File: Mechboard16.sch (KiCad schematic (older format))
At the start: 133 parts, among them CN1 CONN_C16, CN2 CONN_+4, SW0:0 KEY_DEL, SW0:1 KEY_RET, SW0:2 KEY_PND, SW0:3 KEY_HLP, SW0:4 KEY_F1, SW0:5 KEY_F2, SW0:6 KEY_F3, SW0:7 KEY_AT, SW1:0 KEY_3, SW1:1 KEY_W, SW1:2 KEY_A, SW1:3 KEY_4, SW1:4 KEY_Z, SW1:5 KEY_S, SW1:6 KEY_E, SW1:7 KEY_LSH, SW1B:7 KEY_RSH, SW1C:7 KEY_CLK, SW2:0 KEY_5, SW2:1 KEY_R, SW2:2 KEY_D, SW2:3 KEY_6, SW2:4 KEY_C, SW2:5 KEY_F, SW2:6 KEY_T, SW2:7 KEY_X, SW3:0 KEY_7, SW3:1 KEY_Y, SW3:2 KEY_G, SW3:3 KEY_8, SW3:4 KEY_B, SW3:5 KEY_H, SW3:6 KEY_U, SW3:7 KEY_V, SW4:0 KEY_9, SW4:1 KEY_I, SW4:2 KEY_J, SW4:3 KEY_0, SW4:4 KEY_M, SW4:5 KEY_K, SW4:6 KEY_O, SW4:7 KEY_N, SW5:0 KEY_DN, SW5:1 KEY_P, SW5:2 KEY_L, SW5:3 KEY_UP, SW5:4 KEY_DOT, SW5:5 KEY_COL, SW5:6 KEY_MIN, SW5:7 KEY_COM, SW6:0 KEY_LF, SW6:1 KEY_AST, SW6:2 KEY_SEM, SW6:3 KEY_RT, SW6:4 KEY_ESC, SW6:5 KEY_EQ, SW6:6 KEY_PLS, SW6:7 KEY_SLA, SW7:0 KEY_1, SW7:1 KEY_CLR, SW7:2 KEY_CTL, SW7:3 KEY_2, SW7:4 KEY_SPC, SW7:5 KEY_CMD, SW7:6 KEY_Q, SW7:7 KEY_RUN

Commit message: Schematics should be final
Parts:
- added C1, C2: 100n, Capacitor_SMD:C_0805_2012Metric_Pad1.18x1.45mm_HandSolder, symbol Device:C
- added C3: 10n, Capacitor_SMD:C_0805_2012Metric_Pad1.18x1.45mm_HandSolder, symbol Device:C
- added C4: 1u, Capacitor_THT:CP_Radial_D5.0mm_P2.00mm, symbol Device:CP1
- added JP2: JMP_SHIFTLOCK, Connector_PinHeader_2.54mm:PinHeader_2x03_P2.54mm_Vertical, symbol Connector_Generic:Conn_02x03_Odd_Even
- added LD1: LED, LED_THT:LED_D3.0mm, symbol Device:LED
- added R1, R4: 10k, Resistor_SMD:R_0805_2012Metric_Pad1.20x1.40mm_HandSolder, symbol Device:R
- added R2: 100k, Resistor_SMD:R_0805_2012Metric_Pad1.20x1.40mm_HandSolder, symbol Device:R
- added R3: 56, Resistor_SMD:R_0805_2012Metric_Pad1.20x1.40mm_HandSolder, symbol Device:R
- added U1: 4066, Package_SO:SOIC-14_3.9x8.7mm_P1.27mm, symbol 4xxx:4066
- added U2: NE555, Package_SO:SOIC-8_3.9x4.9mm_P1.27mm, symbol Timer:NE555D
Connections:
- net +5V: now also C1.1, C2.1, R1.2, U1.14 (VDD), U2.4 (R), U2.8 (VCC)
- net GND: now also C1.2, C2.2, C3.2, C4.2, LD1.1 (K), R4.1, U1.12, U1.5, U1.6, U1.7 (VSS), U2.1 (GND)
- net col7: now also JP2.4 (Pin_4)
- net row1: now also JP2.3 (Pin_3); no longer SW1C:7.1
- net at D1:7.2 (A), SW1:7.2, SW1B:7.2: no longer SW1C:7.2
- new net: C4.1, JP2.1 (Pin_1), R2.1, SW1C:7.1
- new net: JP2.2 (Pin_2), R1.1, R4.2, SW1C:7.2, U2.2 (TR), U2.6 (THR)
- new net: JP2.6 (Pin_6), U1.1
- new net: R2.2, R3.2, U1.13, U2.3 (Q)
- new net: JP2.5 (Pin_5), U1.2
- new net: LD1.2 (A), R3.1
- new net: C3.1, U2.5 (CV)
- no-connect marks 2 -> 9
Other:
- note added: ""MOMENTARY" TO "LATCHING" CIRCUIT\nFOR THE SHIFT LOCK KEY"
- note added: "Both Shift keys and\nCaps Lock are in parallel\n(But we handle the latter\nseparately so that we can\nuse a non-latching switch)"
- note added: "COMPUTER CONNECTORS"
- note added: "DECOUPLING"
- note added: "KEYBOARD MATRIX"
- note added: "Note that the C16 does not\nhave power on the keyboard\nconnector! A bodge wire mod\nwill be needed!\nFor LittleSixteen, we'll add a\njumper in the next release."
- note added: "SET JP2 ACCORDING TO TYPE\nOF SW1C:7:\n- LATCHING: 1-3 + 2-4\n- MOMENTARY: 3-5 + 4-6"
- note added: "SPARES"
- note added: "Yeah, having the +4 connector here doesn't make much\nsense, since the +4 keyboard uses a totally different form\nfactor, but we get it basically for free and it might still be\ngood for temporary use or whatever."
- moved on the sheet: CN1, CN2, D0:0, D0:1, D0:2, D0:3, D0:4, D0:5, D0:6, D0:7, D1:0, D1:1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

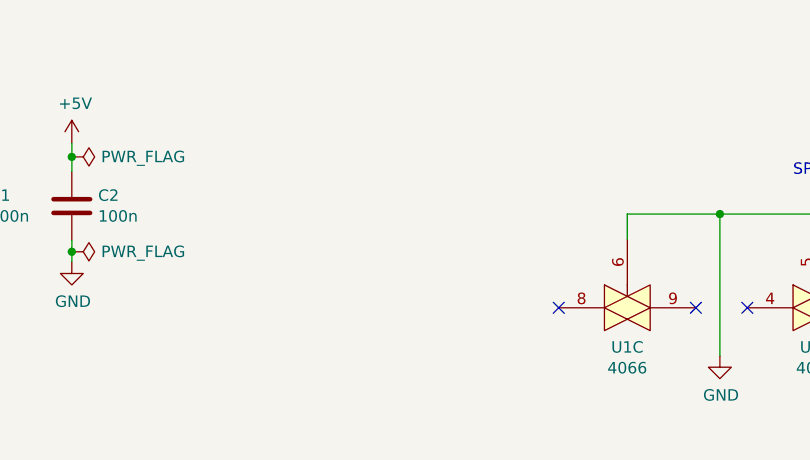
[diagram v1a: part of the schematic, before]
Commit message: Add screw holes
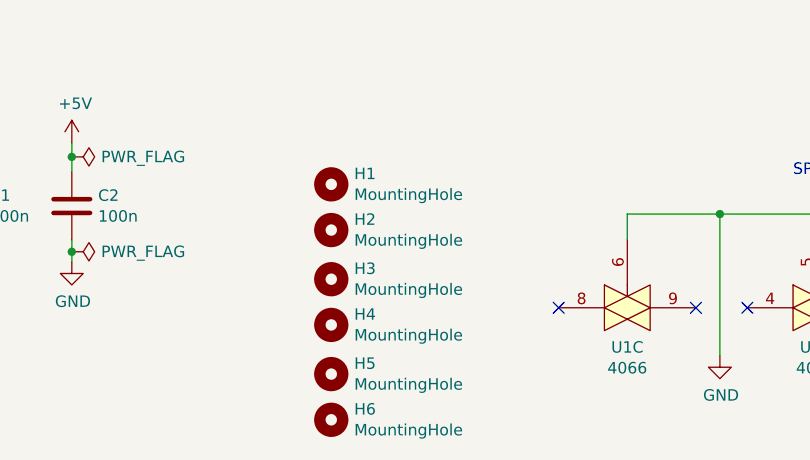
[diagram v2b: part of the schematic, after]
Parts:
- added H1, H2, H3, H4, H5, H6: MountingHole, MountingHole:MountingHole_3.5mm, symbol Mechanical:MountingHole
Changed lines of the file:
@@
 Text Notes 8205 1225 2    50   ~ 0
 Note that the C16 does not\nhave power on the keyboard\nconnector! A bodge wire mod\nwill be needed!\nFor LittleSixteen, we'll add a\njumper in the next release.
+$Comp
+L Mechanical:MountingHole H4
+U 1 1 68545552
+P 3385 7200
+F 0 "H4" H 3485 7246 50  0000 L CNN
+F 1 "MountingHole" H 3485 7155 50  0000 L CNN
+F 2 "MountingHole:MountingHole_3.5mm" H 3385 7200 50  0001 C CNN
+F 3 "~" H 3385 7200 50  0001 C CNN
+	1    3385 7200
+	1    0    0    -1
+$EndComp
+$Comp
+L Mechanical:MountingHole H3
+U 1 1 68546123
+P 3385 7000
+F 0 "H3" H 3485 7046 50  0000 L CNN
+F 1 "MountingHole" H 3485 6955 50  0000 L CNN
+F 2 "MountingHole:MountingHole_3.5mm" H 3385 7000 50  0001 C CNN
+F 3 "~" H 3385 7000 50  0001 C CNN
+	1    3385 7000
+	1    0    0    -1
+$EndComp
+$Comp
+L Mechanical:MountingHole H2
+U 1 1 685466B6
+P 3385 6785
+F 0 "H2" H 3485 6831 50  0000 L CNN
+F 1 "MountingHole" H 3485 6740 50  0000 L CNN
+F 2 "MountingHole:MountingHole_3.5mm" H 3385 6785 50  0001 C CNN
+F 3 "~" H 3385 6785 50  0001 C CNN
+	1    3385 6785
+	1    0    0    -1
+$EndComp
+$Comp
+L Mechanical:MountingHole H1
+U 1 1 68547692
+P 3385 6585
+F 0 "H1" H 3485 6631 50  0000 L CNN
+F 1 "MountingHole" H 3485 6540 50  0000 L CNN
+F 2 "MountingHole:MountingHole_3.5mm" H 3385 6585 50  0001 C CNN
+F 3 "~" H 3385 6585 50  0001 C CNN
+	1    3385 6585
+	1    0    0    -1
+$EndComp
+$Comp
+L Mechanical:MountingHole H6
+U 1 1 685F01A9
+P 3385 7615
+F 0 "H6" H 3485 7661 50  0000 L CNN
+F 1 "MountingHole" H 3485 7570 50  0000 L CNN
+F 2 "MountingHole:MountingHole_3.5mm" H 3385 7615 50  0001 C CNN
+F 3 "~" H 3385 7615 50  0001 C CNN
+	1    3385 7615
+	1    0    0    -1
+$EndComp
+$Comp
+L Mechanical:MountingHole H5
+U 1 1 685F119D
+P 3385 7415
+F 0 "H5" H 3485 7461 50  0000 L CNN
+F 1 "MountingHole" H 3485 7370 50  0000 L CNN
+F 2 "MountingHole:MountingHole_3.5mm" H 3385 7415 50  0001 C CNN
+F 3 "~" H 3385 7415 50  0001 C CNN
+	1    3385 7415
+	1    0    0    -1
+$EndComp
 $EndSCHEMATC

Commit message: Routing done
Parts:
- CN1: footprint Connector_PinHeader_2.54mm:PinHeader_1x20_P2.54mm_Horizontal -> Connector_PinHeader_2.54mm:PinHeader_1x20_P2.54mm_Vertical
- CN2: footprint Connector_PinHeader_2.54mm:PinHeader_1x18_P2.54mm_Horizontal -> Connector_PinHeader_2.54mm:PinHeader_1x18_P2.54mm_Vertical
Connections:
- net col7: no longer JP2.4 (Pin_4)
- net shift_b: now reaches D1:7.2 (A), SW1:7.2, SW1B:7.2
- net shift_b: now also JP2.4 (Pin_4)
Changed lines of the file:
@@
 Comp "SukkoPera"
 Comment1 "Mechanical replacement keyboard for the Commodore 16"
-Comment2 ""
+Comment2 "https://github.com/SukkoPera/MechBoard16"
 Comment3 "Heavily inspired by MechBoard64 by MtnBuffalo"
 Comment4 "https://www.breadbox64.com/blog/the-mechboard64/"
@@
 F 0 "CN2" H 10337 1954 50  0000 R CNN
 F 1 "CONN_+4" H 10337 1863 50  0000 R CNN
-F 2 "Connector_PinHeader_2.54mm:PinHeader_1x18_P2.54mm_Horizontal" H 10365 1980 50  0001 C CNN
+F 2 "Connector_PinHeader_2.54mm:PinHeader_1x18_P2.54mm_Vertical" H 10365 1980 50  0001 C CNN
 F 3 "~" H 10365 1980 50  0001 C CNN
 	1    10365 1980
@@
 F 0 "CN1" H 8977 2054 50  0000 R CNN
 F 1 "CONN_C16" H 8977 1963 50  0000 R CNN
-F 2 "Connector_PinHeader_2.54mm:PinHeader_1x20_P2.54mm_Horizontal" H 9005 2080 50  0001 C CNN
+F 2 "Connector_PinHeader_2.54mm:PinHeader_1x20_P2.54mm_Vertical" H 9005 2080 50  0001 C CNN
 F 3 "~" H 9005 2080 50  0001 C CNN
 	1    9005 2080
@@
 SPARES
 Text Label 10810 4615 2    50   ~ 0
-col7
+shift_b
 Text Label 9705 4615 0    50   ~ 0
-row1
+shift_a
 Wire Wire Line
 	10490 4515 10585 4515
@@
 	1    0    0    -1
 $EndComp
+Text Label 5675 1835 2    50   ~ 0
+shift_a
+Text Label 5875 2235 2    50   ~ 0
+shift_b
 $EndSCHEMATC

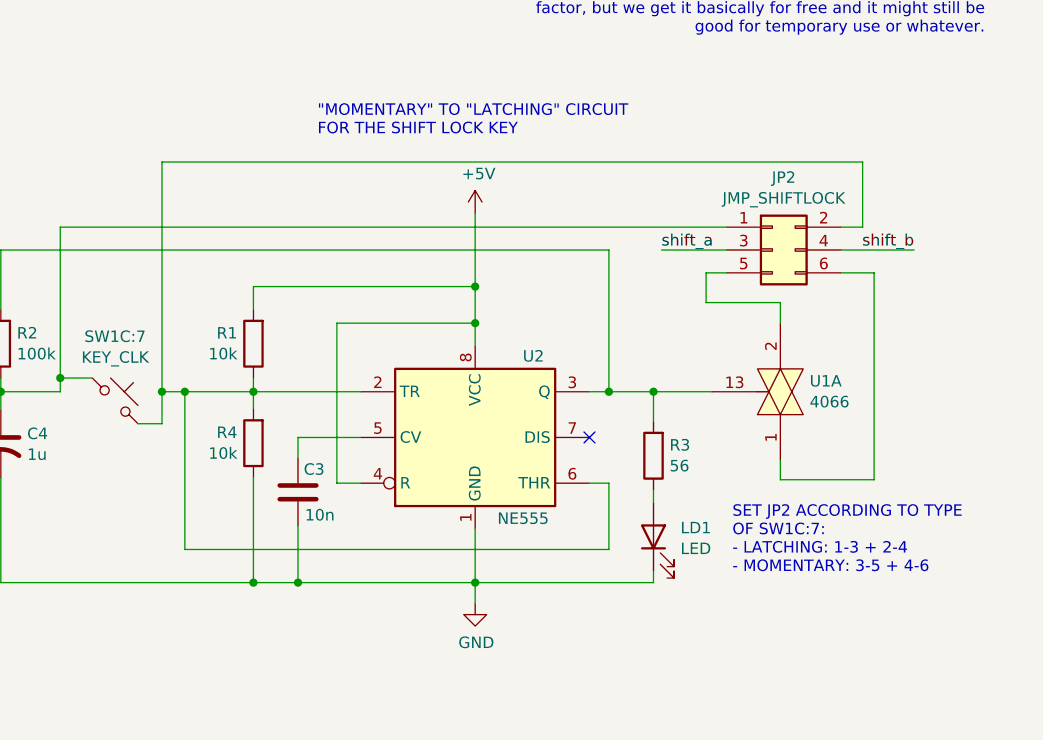
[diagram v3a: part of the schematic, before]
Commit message: Change JP2 to solder jumper(s)
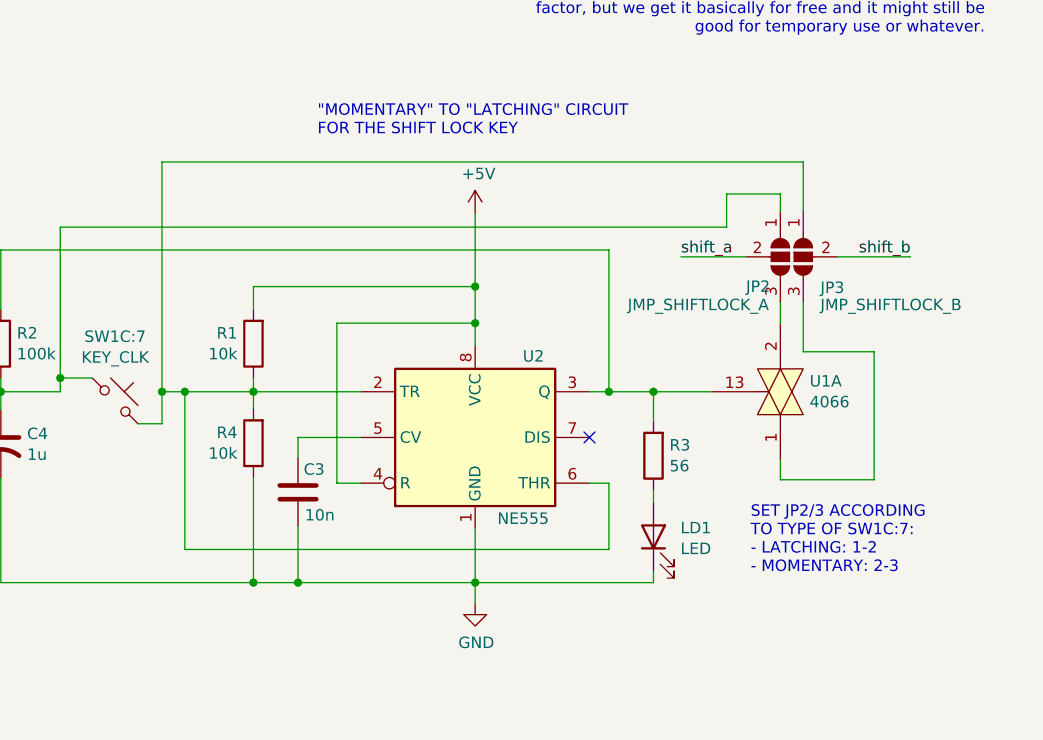
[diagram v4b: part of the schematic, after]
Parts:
- removed JP2: JMP_SHIFTLOCK, Connector_PinHeader_2.54mm:PinHeader_2x03_P2.54mm_Vertical, symbol Connector_Generic:Conn_02x03_Odd_Even
- added JP2: JMP_SHIFTLOCK_A, Jumper:SolderJumper-3_P1.3mm_Open_RoundedPad1.0x1.5mm, symbol Jumper:SolderJumper_3_Open
- added JP3: JMP_SHIFTLOCK_B, Jumper:SolderJumper-3_P1.3mm_Open_RoundedPad1.0x1.5mm, symbol Jumper:SolderJumper_3_Open
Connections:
- net row1: now also JP3.2 (C)
- net shift_b: now also JP2.2 (C)
- net at C4.1, R2.1, SW1C:7.1: now also JP3.1 (A)
- net at R1.1, R4.2, SW1C:7.2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: now also JP2.1 (A)
- net at U1.1: now also JP2.3 (B)
- net at U1.2: now also JP3.3 (B)
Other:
- note added: "SET JP2/3 ACCORDING\nTO TYPE OF SW1C:7:\n- LATCHING: 1-2\n- MOMENTARY: 2-3"
- note removed: "SET JP2 ACCORDING TO TYPE\nOF SW1C:7:\n- LATCHING: 1-3 + 2-4\n- MOMENTARY: 3-5 + 4-6"
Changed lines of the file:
@@
-	1    0    0    -1
-$EndComp
-$Comp
-L Connector_Generic:Conn_02x03_Odd_Even JP2
-U 1 1 66C6616E
-P 10190 4615
-F 0 "JP2" H 10240 4932 50  0000 C CNN
-F 1 "JMP_SHIFTLOCK" H 10240 4841 50  0000 C CNN
-F 2 "Connector_PinHeader_2.54mm:PinHeader_2x03_P2.54mm_Vertical" H 10190 4615 50  0001 C CNN
-F 3 "~" H 10190 4615 50  0001 C CNN
-	1    10190 4615
 	1    0    0    -1
 $EndComp
@@
 Text Notes 5405 6555 0    50   ~ 0
 SPARES
-Text Label 10810 4615 2    50   ~ 0
+Text Label 10795 4645 2    50   ~ 0
 shift_b
-Text Label 9705 4615 0    50   ~ 0
+Text Label 9790 4645 0    50   ~ 0
 shift_a
 Wire Wire Line
-	10490 4515 10585 4515
-Wire Wire Line
-	10585 4515 10585 4230
-Wire Wire Line
-	10490 4615 10810 4615
-Wire Wire Line
-	9990 4615 9705 4615
+	10475 4645 10795 4645
+Wire Wire Line
+	10075 4645 9790 4645
 Text Notes 8695 655  0    50   ~ 0
 COMPUTER CONNECTORS
@@
 Connection ~ 7620 5235
 Wire Wire Line
-	9990 4715 9900 4715
-Wire Wire Line
-	9900 4715 9900 4845
-Wire Wire Line
-	9900 4845 10225 4845
-Wire Wire Line
 	10225 4845 10225 4935
-Wire Wire Line
-	10490 4715 10635 4715
-Wire Wire Line
-	10635 4715 10635 5620
 Wire Wire Line
 	10635 5620 10225 5620
@@
 	7520 5235 7520 4230
 Wire Wire Line
-	7520 4230 10585 4230
+	7520 4230 10325 4230
 Connection ~ 7520 5235
-Text Notes 10015 6035 0    50   ~ 0
-SET JP2 ACCORDING TO TYPE\nOF SW1C:7:\n- LATCHING: 1-3 + 2-4\n- MOMENTARY: 3-5 + 4-6
+Text Notes 10095 6035 0    50   ~ 0
+SET JP2/3 ACCORDING\nTO TYPE OF SW1C:7:\n- LATCHING: 1-2\n- MOMENTARY: 2-3
 $Comp
 L power:PWR_FLAG #FLG0101
@@
 Text Label 5875 2235 2    50   ~ 0
 shift_b
+$Comp
+L Jumper:SolderJumper_3_Open JP2
+U 1 1 68A0CA63
+P 10325 4645
+F 0 "JP2" V 10455 4790 50  0000 L CNN
+F 1 "JMP_SHIFTLOCK_A" V 10535 4795 50  0000 L CNN
+F 2 "Jumper:SolderJumper-3_P1.3mm_Open_RoundedPad1.0x1.5mm" H 10325 4645 50  0001 C CNN
+F 3 "~" H 10325 4645 50  0001 C CNN
+	1    10325 4645
+	0    -1   1    0
+$EndComp
+Wire Wire Line
+	10325 4845 10325 5060
+Wire Wire Line
+	10325 5060 10635 5060
+Wire Wire Line
+	10635 5060 10635 5620
+Wire Wire Line
+	10225 4445 10225 4370
+Wire Wire Line
+	10225 4370 9990 4370
+Wire Wire Line
+	9990 4370 9990 4515
+Wire Wire Line
+	10325 4445 10325 4230
+$Comp
+L Jumper:SolderJumper_3_Open JP3
+U 1 1 68958908
+P 10225 4645
+F 0 "JP3" V 10360 4820 50  0000 L CNN
+F 1 "JMP_SHIFTLOCK_B" V 10435 4820 50  0000 L CNN
+F 2 "Jumper:SolderJumper-3_P1.3mm_Open_RoundedPad1.0x1.5mm" H 10225 4645 50  0001 C CNN
+F 3 "~" H 10225 4645 50  0001 C CNN
+	1    10225 4645
+	0    1    1    0
+$EndComp
 $EndSCHEMATC

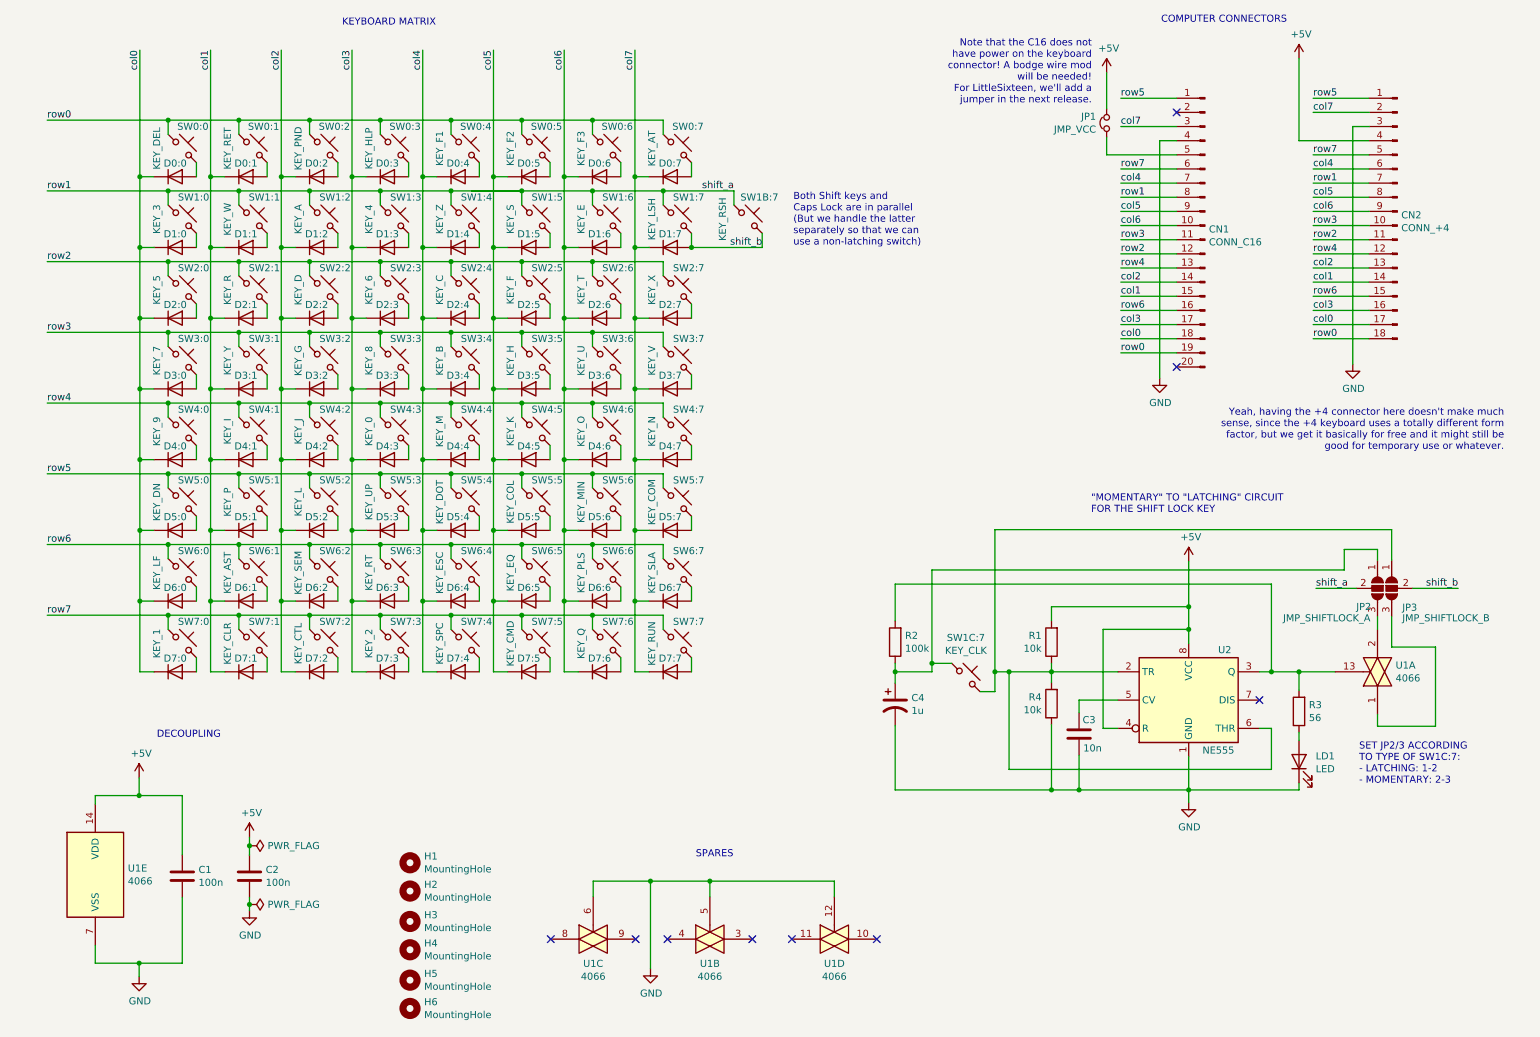
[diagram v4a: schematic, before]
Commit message: Add RP2040 board so that keybord can be used as a HID device
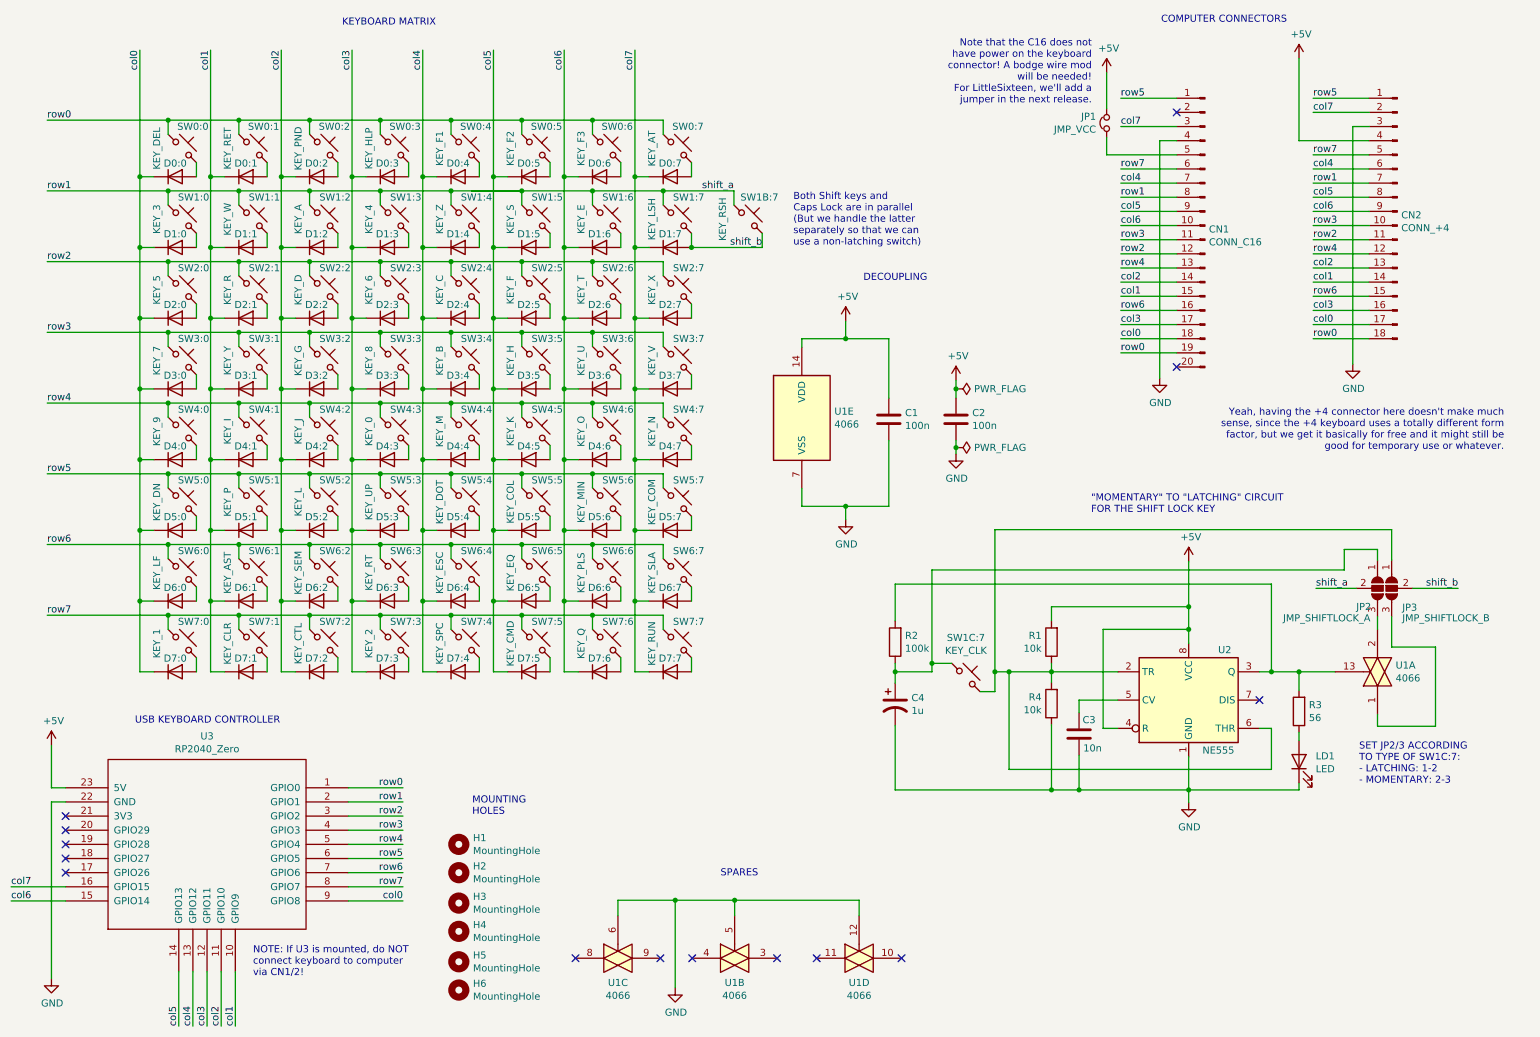
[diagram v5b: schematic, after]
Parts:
- added U3: RP2040_Zero, Mechboard16:rp2040-zero, symbol RP2040_Zero:RP2040_Zero
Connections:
- net +5V: now also U3.23 (5V)
- net GND: now also U3.22 (GND)
- net col0: now also U3.9 (GPIO8)
- net col1: now also U3.10 (GPIO9)
- net col2: now also U3.11 (GPIO10)
- net col3: now also U3.12 (GPIO11)
- net col4: now also U3.13 (GPIO12)
- net col5: now also U3.14 (GPIO13)
- net col6: now also U3.15 (GPIO14)
- net col7: now also U3.16 (GPIO15)
- net row0: now also U3.1 (GPIO0)
- net row1: now also U3.2 (GPIO1)
- net row2: now also U3.3 (GPIO2)
- net row3: now also U3.4 (GPIO3)
- net row4: now also U3.5 (GPIO4)
- net row5: now also U3.6 (GPIO5)
- net row6: now also U3.7 (GPIO6)
- net row7: now also U3.8 (GPIO7)
- no-connect marks 9 -> 14
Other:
- note added: "MOUNTING\nHOLES"
- note added: "NOTE: If U3 is mounted, do NOT \nconnect keyboard to computer\nvia CN1/2!"
- note added: "USB KEYBOARD CONTROLLER"
- moved on the sheet: C1, C2, H1, H2, H3, H4, H5, H6, U1B, U1C, U1D, U1E

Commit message: Add LCSC P/Ns
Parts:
- C1, C2: LCSC (none) -> C49678
- C3: LCSC (none) -> C1710
- D0:0, D0:1, D0:2, D0:3, D0:4, D0:5, D0:6, D0:7, D1:0, D1:1, D1:2, D1:3, D1:4, D1:5, D1:6, D1:7, D2:0, D2:1, D2:2, D2:3, D2:4, D2:5, D2:6, D2:7, D3:0, D3:1, D3:2, D3:3, D3:4, D3:5, D3:6, D3:7, D4:0, D4:1, D4:2, D4:3, D4:4, D4:5, D4:6, D4:7, D5:0, D5:1, D5:2, D5:3, D5:4, D5:5, D5:6, D5:7, D6:0, D6:1, D6:2, D6:3, D6:4, D6:5, D6:6, D6:7, D7:0, D7:1, D7:2, D7:3, D7:4, D7:5, D7:6, D7:7: LCSC (none) -> C2128
- H1, H2, H3, H4, H5, H6: LCSC (none) -> -
- R1, R4: LCSC (none) -> C17414
- R2: LCSC (none) -> C149504
- R3: LCSC (none) -> C17557
- U1: LCSC (none) -> C412482
- U2: LCSC (none) -> C181735
